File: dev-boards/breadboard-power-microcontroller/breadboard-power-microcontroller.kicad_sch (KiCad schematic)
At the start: 25 parts, among them J0 USB_C_Receptacle_PowerOnly_6P, J1 Barrel_Jack_Switch, J2 Conn_01x02, Q1 AO3401A, Q2 AO3401A, SW1 SW_DPDT_x2, U1 AMS1117-5.0, U2 AMS1117-3.3

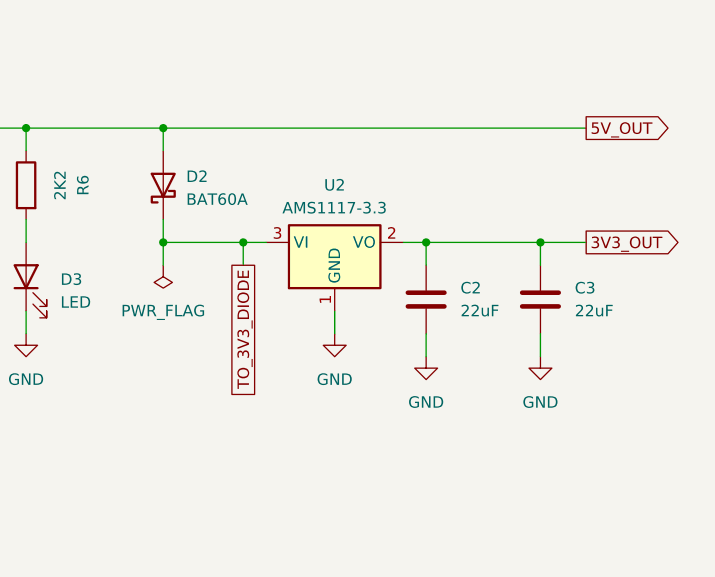
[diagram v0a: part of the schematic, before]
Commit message: Replace AMS1117 with MT6211 on breadboard microcontroller power board
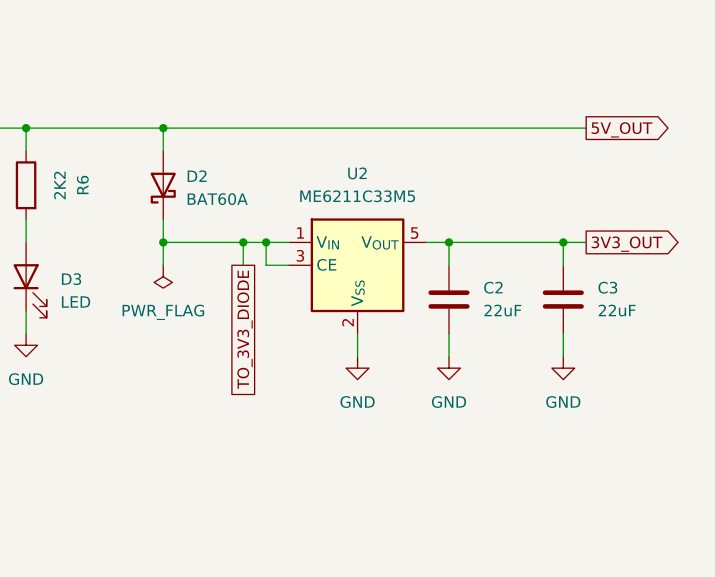
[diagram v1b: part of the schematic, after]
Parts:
- removed U2: AMS1117-3.3, Package_TO_SOT_SMD:SOT-223-3_TabPin2, symbol Regulator_Linear:AMS1117-3.3
- added U2: ME6211C33M5, custom:SOT-23-5_HandSoldering_simple, symbol Regulator_Linear:ME6211C33M5
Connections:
- net 3V3_OUT: now also U2.5 (V_{OUT})
- net GND: now also U2.2 (V_{SS})
- net TO_3V3_DIODE: now also U2.1 (V_{IN}), U2.3 (CE)
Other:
- moved on the sheet: C2, C3
